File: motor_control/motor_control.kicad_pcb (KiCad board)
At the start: 4 copper layers, 75 x 56 mm, 28 parts, among them J1 GPIO, J2 MotA, J3 MotB, J4 MOT_POW, J5 UART, J6 SPI, J7 I2C, J8 VBUS_OUT, SW1 PU, SW2 PD, U1 HC-SR04

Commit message: add bear head logo
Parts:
- added G***: LOGO, LOGO, F.Cu at (111.4, 91.4)
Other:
- board text added: "Motor Control 25.08"

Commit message: adjust labels
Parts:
- A2: value Pololu_Breakout_TB6612FNG -> TB6612FNG
- A3: value RaspberryPi_Pico -> Raspberry Pi Pico
- renumbered D1 to BGKR
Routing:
- net /PULLUP: track 17.4 -> 23.9 mm
- net /PULLDOWN: track 16.2 -> 22.7 mm
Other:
- board text added: "+"
- board text added: "-"
- board text removed: "A1"
- board text removed: "A2"
- board text removed: "B1"
- board text removed: "B2"
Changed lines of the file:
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@@
 		)
 		(property "Value" "HC-SR04"
-			(at 23.8102 3.370695 90)
-			(layer "F.Fab")
+			(at 8.7 1.8 90)
+			(layer "F.SilkS")
 			(effects
 				(font
-					(size 1.001693 1.001693)
+					(size 1 1)
 					(thickness 0.15)
 				)
@@
 			)
 		)
-		(property "Value" "Pololu_Breakout_TB6612FNG"
-			(at 1.7955 -0.455 90)
-			(layer "F.Fab")
+		(property "Value" "TB6612FNG"
+			(at 0.0955 2.545 180)
+			(layer "F.SilkS")
 			(effects
 				(font
-					(size 0.640105 0.640105)
+					(size 0.8 0.8)
 					(thickness 0.15)
 				)
@@
 				(font
 					(size 1 1)
-					(thickness 0.15)
+					(thickness 0.2)
+					(bold yes)
 				)
 				(justify left)
 			)
 		)
-		(property "Value" "RaspberryPi_Pico"
+		(property "Value" "Raspberry Pi Pico"
 			(at 2.766 0.116 0)
 			(unlocked yes)
-			(layer "F.Fab")
+			(layer "F.SilkS")
 			(effects
 				(font
@@
 		(descr "LED, diameter 5.0mm, 4 pins, WP154A4, https://www.kingbright.com/attachments/file/psearch/000/00/00/L-154A4SUREQBFZGEW(Ver.11A).pdf")
 		(tags "LED diameter 5.0mm 2 pins diameter 5.0mm 3 pins diameter 5.0mm 4 pins RGB RGBLED")
-		(property "Reference" "D1"
-			(at 2.921 -3.937 0)
+		(property "Reference" "BGKR"
+			(at 3.12 -3.98 0)
 			(layer "F.SilkS")
 			(effects
@@
 		)
 		(property "Value" "LED_RKGB"
-			(at 3.2385 -3.937 0)
+			(at 2.92 -3.98 0)
 			(layer "F.Fab")
 			(effects
@@
 		(tags "Through hole pin header THT 1x02 2.54mm single row")
 		(property "Reference" "J8"
-			(at -2.6 3.6434 270)
+			(at 0.8 5.0434 0)
 			(layer "F.SilkS")
 			(effects
@@
 		(layer "Edge.Cuts")
 	)
-	(gr_text "A2"
-		(at 109.160691 58.5 0)
+	(gr_text "AO2"
+		(at 109 58.5 0)
 		(layer "F.SilkS")
 		(effects
@@
 		)
 	)
-	(gr_text "A1"
-		(at 96.460691 58.5 0)
+	(gr_text "AO1"
+		(at 96.2 58.5 0)
 		(layer "F.SilkS")
 		(effects
@@
 		)
 	)
-	(gr_text "VMOT"
-		(at 91.8 89.5 0)
+	(gr_text "+"
+		(at 91.8 89.3 0)
 		(layer "F.SilkS")
 		(effects
 			(font
-				(size 0.8 0.8)
+				(size 1 1)
 				(thickness 0.15)
 			)
@@
 		)
 	)
-	(gr_text "GND"
-		(at 94.9 89.5 0)
+	(gr_text "-"
+		(at 94.5 89.4 0)
 		(layer "F.SilkS")
 		(effects
 			(font
-				(size 0.8 0.8)
+				(size 1 1)
 				(thickness 0.15)
 			)
@@
 		)
 	)
-	(gr_text "B2"
-		(at 109.2 86.2 0)
+	(gr_text "BO2"
+		(at 108.9 86.2 0)
 		(layer "F.SilkS")
 		(effects
@@
 			(font
 				(size 1 1)
-				(thickness 0.15)
+				(thickness 0.2)
+				(bold yes)
 			)
 			(justify bottom)
@@
 	)
 	(gr_text "VBUS"
-		(at 159.005 82.9 0)
+		(at 159.3 82.9 0)
+		(layer "F.SilkS")
+		(effects
+			(font
+				(size 1 1)
+				(thickness 0.15)
+			)
+		)
+	)
+	(gr_text "GND"
+		(at 159.7 85.7 0)
 		(layer "F.SilkS")
 		(effects
@@
 		)
 	)
-	(gr_text "B1"
-		(at 96.5 86.2 0)
+	(gr_text "BO1"
+		(at 96.1 86.2 0)
 		(layer "F.SilkS")
 		(effects
@@
 	)
 	(segment
+		(start 118.64 93.6)
+		(end 125.14 93.6)
+		(width 0.2)
+		(layer "F.Cu")
+		(net 55)
+	)
+	(segment
 		(start 125.146 86.992)
 		(end 130.005 82.133)
@@
 	)
 	(segment
+		(start 128.8 93.6)
+		(end 135.3 93.6)
+		(width 0.2)
+		(layer "F.Cu")
+		(net 58)
+	)
+	(segment

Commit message: final tweak pcb
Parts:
- moved J4 2.93 mm to (97.3, 90.9)
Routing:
- net VMOT: track 18.8 -> 17.0 mm
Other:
- board text added: "JLCJLCJLC"
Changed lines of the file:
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@@
 	(footprint "Connector_PinHeader_2.54mm:PinHeader_1x02_P2.54mm_Horizontal"
 		(layer "F.Cu")
-		(at 94.4882 91.8974 -90)
+		(at 97.2545 90.945 -90)
 		(descr "Through hole angled pin header, 1x02, 2.54mm pitch, 6mm pin length, single row")
 		(tags "Through hole angled pin header THT 1x02 2.54mm single row")
 		(property "Reference" "J4"
-			(at 2.9026 -2.7178 180)
+			(at 2.755 5.3545 0)
 			(layer "F.SilkS")
 			(effects
@@
 		)
 		(property "Value" "MOT_POW"
-			(at -2.54 1.0922 180)
-			(layer "F.Fab")
+			(at -2.54 1.0922 0)
+			(layer "F.SilkS")
 			(effects
 				(font
@@
 		(tags "tact sw push 6mm")
 		(property "Reference" "SW1"
-			(at 3.25 2.25 0)
+			(at -3.04 5.4 0)
 			(layer "F.SilkS")
 			(effects
 				(font
-					(size 1 1)
+					(size 0.8 0.8)
 					(thickness 0.15)
 				)
@@
 		(tags "tact sw push 6mm")
 		(property "Reference" "SW2"
-			(at 3.25 2.25 0)
+			(at -2.8 -1 0)
 			(layer "F.SilkS")
 			(effects
 				(font
-					(size 1 1)
+					(size 0.8 0.8)
 					(thickness 0.15)
 				)
@@
 		(tags "LED diameter 5.0mm 2 pins diameter 5.0mm 3 pins diameter 5.0mm 4 pins RGB RGBLED")
 		(property "Reference" "BGKR"
-			(at 3.12 -3.98 0)
+			(at 1.72 -3.98 0)
 			(layer "F.SilkS")
 			(effects
@@
 	)
 	(gr_text "+"
-		(at 91.8 89.3 0)
+		(at 92.1 89.5 0)
 		(layer "F.SilkS")
 		(effects
@@
 	)
 	(gr_text "-"
-		(at 94.5 89.4 0)
+		(at 100 89.4 0)
 		(layer "F.SilkS")
 		(effects
@@
 	)
 	(gr_text "Motor Control\n25.08"
-		(at 112 97.9 0)
+		(at 111.9 97.9 0)
 		(layer "F.SilkS")
 		(effects
@@
 		)
 	)
+	(gr_text "JLCJLCJLC"
+		(at 107.4 92.7 0)
+		(layer "B.SilkS")
+		(effects
+			(font
+				(size 1 1)
+				(thickness 0.15)
+			)
+			(justify left bottom mirror)
+		)
+	)
 	(gr_text "USB"
 		(at 177.724 71.552 0)
@@
 	)
 	(segment
-		(start 95.4 88.4456)
-		(end 95.4 76.9)
+		(start 95.5645 77.395)
+		(end 97.2545 75.705)
 		(width 0.4)
 		(layer "B.Cu")
@@
 	)
 	(segment
-		(start 95.4 76.9)
-		(end 96.595 75.705)
+		(start 94.7145 90.945)
+		(end 95.5645 90.095)
 		(width 0.4)
 		(layer "B.Cu")
@@
 	)
 	(segment
-		(start 91.9482 91.8974)
-		(end 95.4 88.4456)
+		(start 95.5645 90.095)
+		(end 95.5645 77.395)
 		(width 0.4)
 		(layer "B.Cu")

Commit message: export gerber
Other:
- board text added: "JLCJLCJLCJLC"
- board text removed: "JLCJLCJLC"
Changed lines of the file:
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@@
 		(grid_origin 100 100)
 		(pcbplotparams
-			(layerselection 0x00000000_00000000_00000000_000000a5)
+			(layerselection 0x00000000_00000000_55555555_5755f5af)
 			(plot_on_all_layers_selection 0x00000000_00000000_00000000_00000000)
 			(disableapertmacros no)
@@
 			(sketchdnponfab yes)
 			(crossoutdnponfab yes)
-			(subtractmaskfromsilk no)
+			(subtractmaskfromsilk yes)
 			(outputformat 1)
 			(mirror no)
-			(drillshape 1)
+			(drillshape 0)
 			(scaleselection 1)
-			(outputdirectory "")
+			(outputdirectory "jlcpcb_gerbers/")
 		)
 	)
@@
 		)
 	)
-	(gr_text "JLCJLCJLC"
-		(at 107.4 92.7 0)
+	(gr_text "JLCJLCJLCJLC"
+		(at 91.4 55.8 270)
 		(layer "B.SilkS")
 		(effects

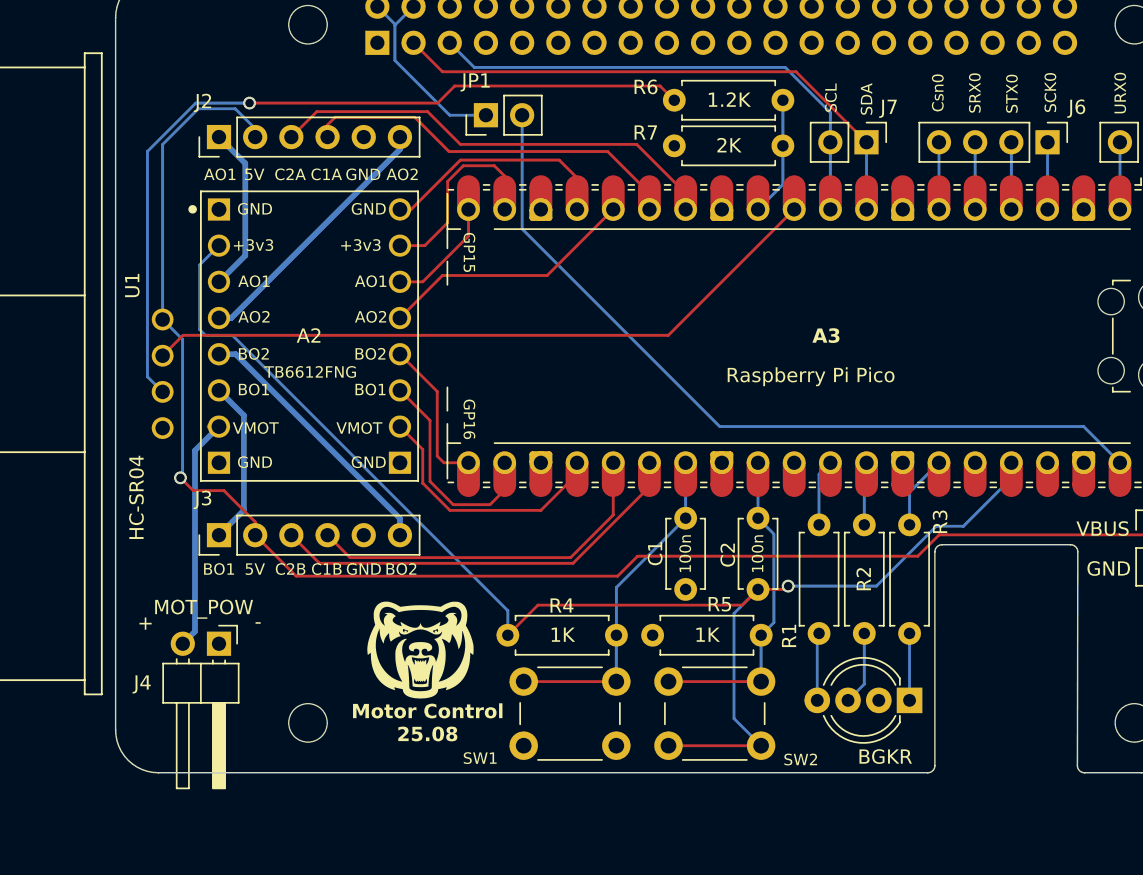
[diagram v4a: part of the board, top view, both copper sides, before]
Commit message: update schematic and pcb
1. added a input 01x02 header for PEB power up +5V
2. switched to +5V to power up sonar and encoders
3. set jumper between +5V and PEB 5V input
4. upgraded motor driver input to JST-XH
5. updated footprints
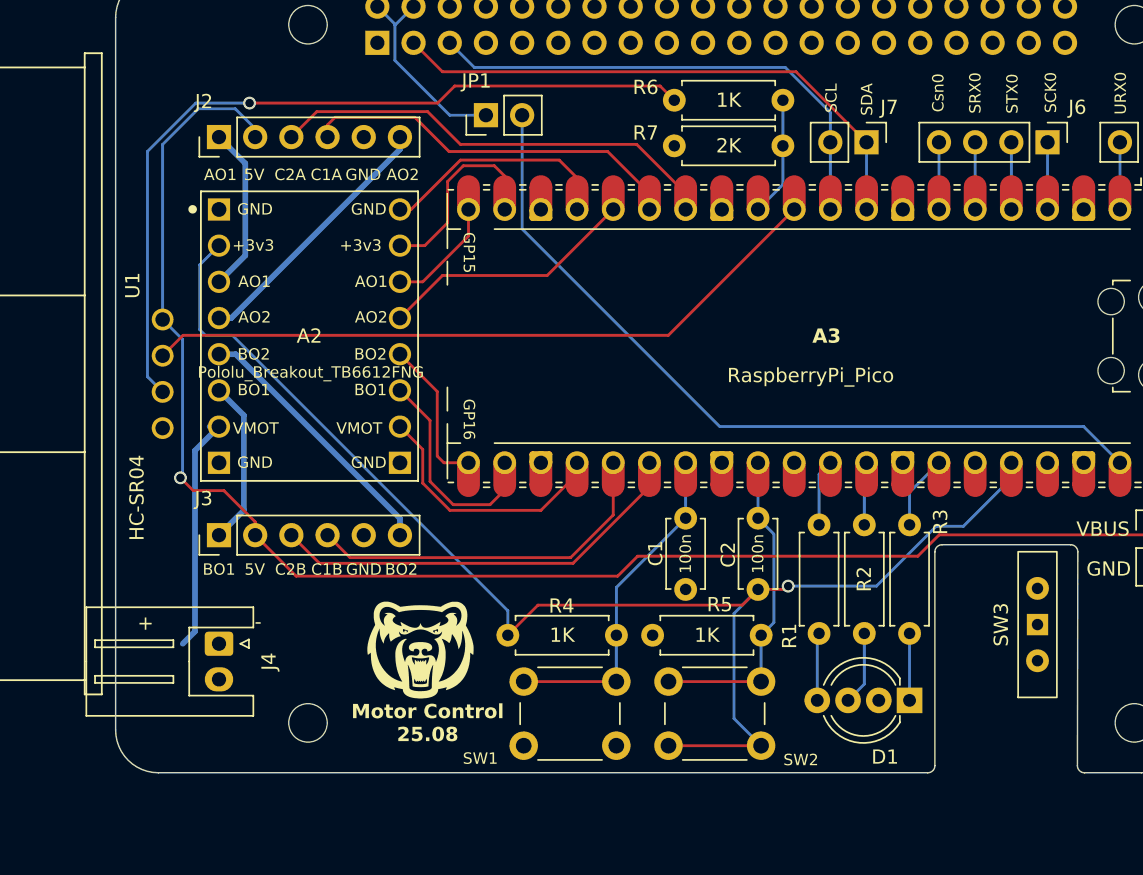
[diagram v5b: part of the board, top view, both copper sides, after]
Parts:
- added SW3: SW_SPDT_312, Button_Switch_THT:SW_Slide-03_Wuerth-WS-SLTV_10x2.5x6.4_P2.54mm, F.Cu at (154.7, 89.6)
- A2: value TB6612FNG -> Pololu_Breakout_TB6612FNG
- A3: value Raspberry Pi Pico -> RaspberryPi_Pico
- J4: footprint Connector_PinHeader_2.54mm:PinHeader_1x02_P2.54mm_Horizontal -> Connector_JST:JST_XH_S2B-XH-A_1x02_P2.50mm_Horizontal
- J8: value VBUS_OUT -> PEB_5V_IN
- JP1: value 5V_VBUS -> 5V_PEB_RPi
- R6: value 1.2K -> 1K
- renumbered BGKR to D1
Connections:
- J2 pad 2: VBUS -> +5V
- J3 pad 2: VBUS -> +5V
- J8 pad 1: VBUS -> 5V_IN
- JP1 pad 1: +5V -> 5V_IN
- JP1 pad 2: VSYS -> +5V
- R7 pad 1: GND -> Net-(U1-ECHO)
- R7 pad 2: /ECHO -> GND
- U1 pad 1: VBUS -> +5V

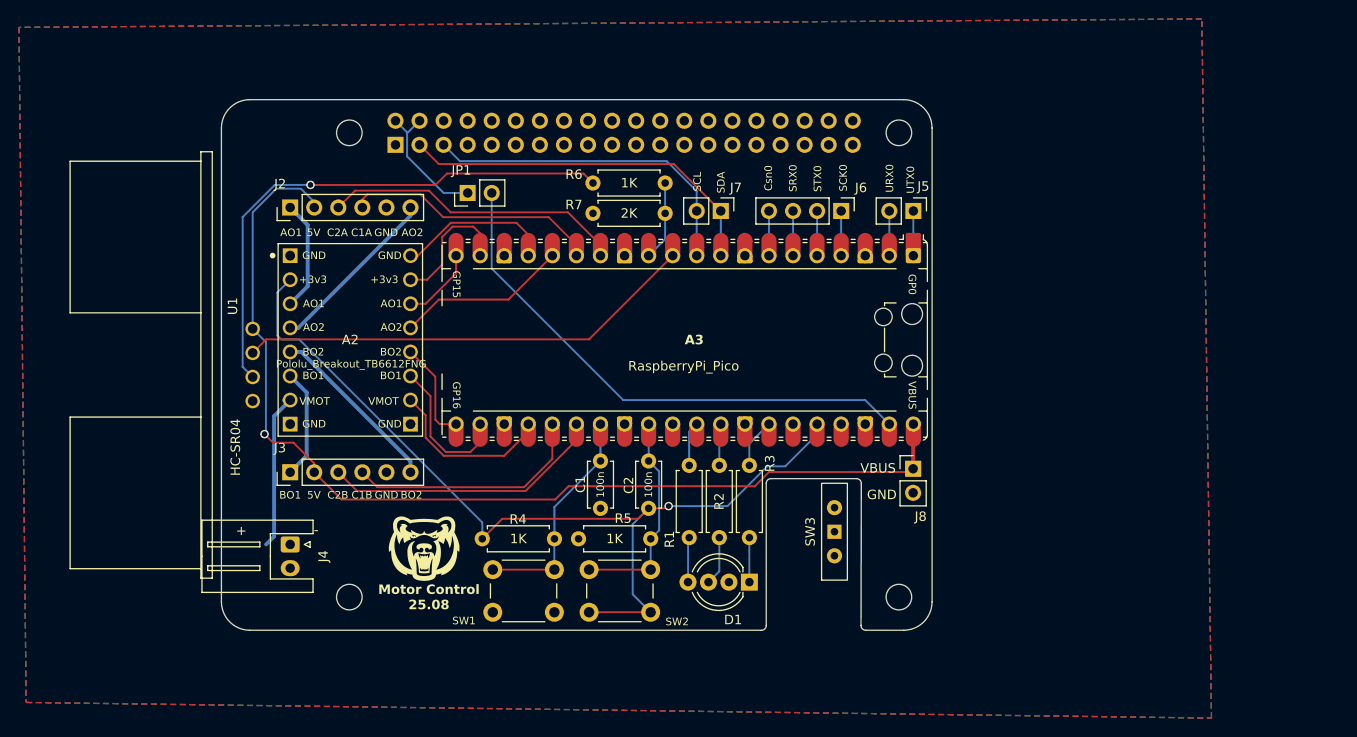
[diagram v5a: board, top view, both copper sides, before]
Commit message: fix j9 footprint and update pcb
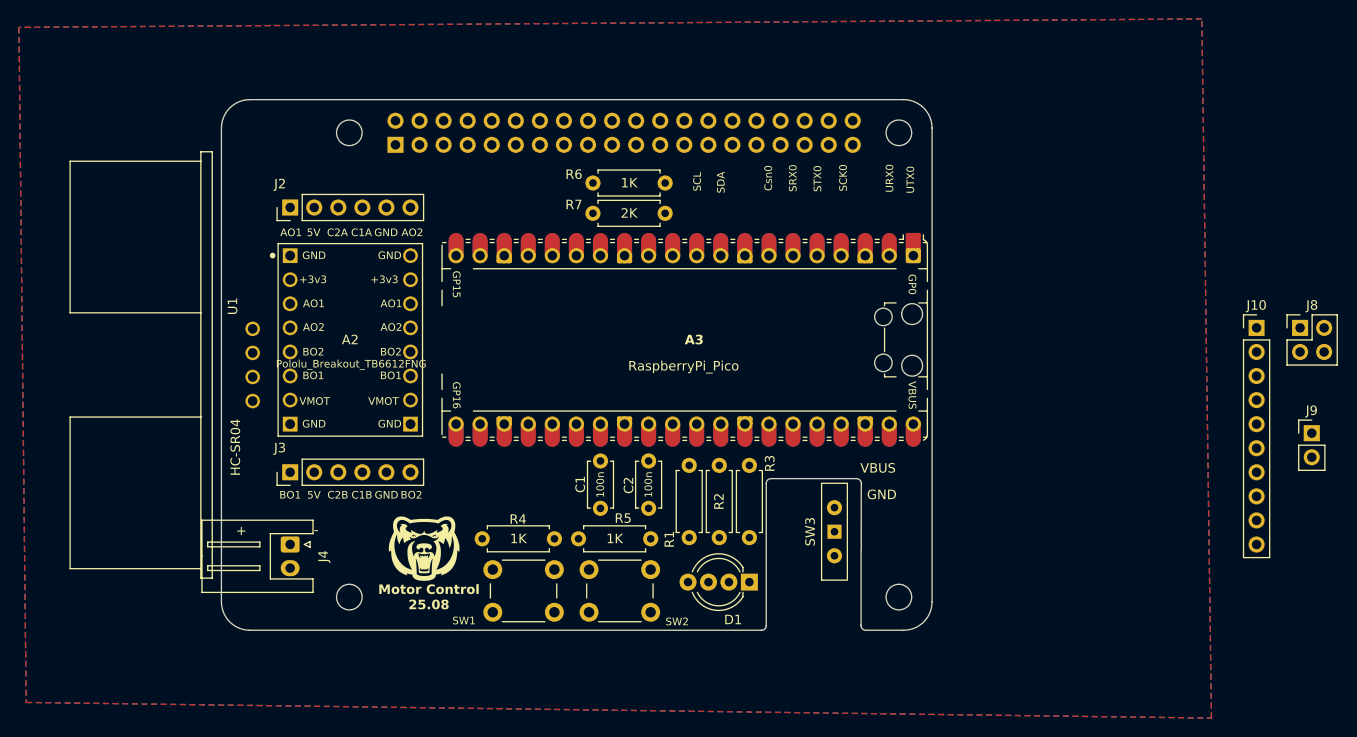
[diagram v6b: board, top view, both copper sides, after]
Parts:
- removed J5: UART, Connector_PinHeader_2.54mm:PinHeader_1x02_P2.54mm_Vertical
- removed J6: SPI, Connector_PinHeader_2.54mm:PinHeader_1x04_P2.54mm_Vertical
- removed J7: I2C, Connector_PinHeader_2.54mm:PinHeader_1x02_P2.54mm_Vertical
- removed JP1: 5V_PEB_RPi, Connector_PinHeader_2.54mm:PinHeader_1x02_P2.54mm_Vertical
- added J10: Conn_01x10_Pin, Connector_PinHeader_2.54mm:PinHeader_1x10_P2.54mm_Vertical, F.Cu at (199.2, 68.1)
- added J9: VBUS_OUT, Connector_PinHeader_2.54mm:PinHeader_1x02_P2.54mm_Vertical, F.Cu at (205.1, 79.2)
- J8: value PEB_5V_IN -> Conn_02x02_Odd_Even; footprint Connector_PinHeader_2.54mm:PinHeader_1x02_P2.54mm_Vertical -> Connector_PinHeader_2.54mm:PinHeader_2x02_P2.54mm_Vertical
- moved J8 43.5 mm to (203.8, 68.1)
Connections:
- A3 pad 1: /UART0_TX -> /GP0
- A3 pad 10: /SCL1 -> /GP7
- A3 pad 16: /STBY -> /PWMA
- A3 pad 17: /PWMA -> /AIN2
- A3 pad 19: /AIN2 -> /AIN1
- A3 pad 2: /UART0_RX -> /GP1
- A3 pad 20: /AIN1 -> /STBY
- A3 pad 25: /C1B -> /C2B
- A3 pad 26: /C2B -> /C1B
- A3 pad 4: /SPI0_SCK -> /GP2
- A3 pad 5: /SPI0_TX -> /GP3
- A3 pad 6: /SPI0_RX -> /GP4
- A3 pad 7: /SPI0_CSn -> /GP5
- A3 pad 9: /SDA1 -> /GP6
- C1 pad 1: GND -> /PULLUP
- C1 pad 2: /PULLUP -> GND
- C2 pad 1: /PULLDOWN -> GND
- C2 pad 2: +3V3 -> /PULLDOWN
- J2 pad 2: +5V -> REG_5V
- J3 pad 2: +5V -> REG_5V
- J8 pad 1: 5V_IN -> GND
- J8 pad 2: GND -> REG_5V
- SW1 pad 1: /PULLUP -> GND
- SW1 pad 2: GND -> /PULLUP
- SW3 pad 1: 5V_IN -> REG_5V
- U1 pad 1: +5V -> REG_5V
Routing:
- net VBUS: track 110.7 -> 0.00 mm, vias 1 -> 0
- net +3V3: track 97.9 -> 0.00 mm, vias 1 -> 0
- net Net-(U1-ECHO): track 56.9 -> 0.00 mm, vias 1 -> 0
- net VSYS: track 56.7 -> 0.00 mm
- net /TRIG: track 48.6 -> 0.00 mm
- net /SDA1: track 39.4 -> 0.00 mm
- net /SCL1: track 35.5 -> 0.00 mm
- net /C2A: track 31.9 -> 0.00 mm
- net /C2B: track 29.2 -> 0.00 mm
- net /C1A: track 27.0 -> 0.00 mm
- net /C1B: track 24.8 -> 0.00 mm
- net /PULLUP: track 23.9 -> 0.00 mm
- net /PULLDOWN: track 22.7 -> 0.00 mm
- net /BO2: track 18.6 -> 0.00 mm
- net /AO2: track 18.5 -> 0.00 mm
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
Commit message: update motor connector pins
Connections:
- J2 pad 3: /C2A -> /C1A
- J2 pad 4: /C1A -> /C2A
- J3 pad 1: /BO1 -> /BO2
- J3 pad 3: /C2B -> /C1B
- J3 pad 4: /C1B -> /C2B
- J3 pad 6: /BO2 -> /BO1
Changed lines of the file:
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@@
 			(layers "*.Cu" "*.Mask")
 			(remove_unused_layers no)
-			(net 40 "/BO1")
+			(net 32 "/BO2")
 			(pinfunction "Pin_1")
 			(pintype "passive")
@@
 			(layers "*.Cu" "*.Mask")
 			(remove_unused_layers no)
-			(net 65 "/C2B")
+			(net 60 "/C1B")
 			(pinfunction "Pin_3")
 			(pintype "passive")
@@
 			(layers "*.Cu" "*.Mask")
 			(remove_unused_layers no)
-			(net 60 "/C1B")
+			(net 65 "/C2B")
 			(pinfunction "Pin_4")
 			(pintype "passive")
@@
 			(layers "*.Cu" "*.Mask")
 			(remove_unused_layers no)
-			(net 32 "/BO2")
+			(net 40 "/BO1")
 			(pinfunction "Pin_6")
 			(pintype "passive")
@@
 			(layers "*.Cu" "*.Mask")
 			(remove_unused_layers no)
-			(net 59 "/C2A")
+			(net 44 "/C1A")
 			(pinfunction "Pin_3")
 			(pintype "passive")
@@
 			(layers "*.Cu" "*.Mask")
 			(remove_unused_layers no)
-			(net 44 "/C1A")
+			(net 59 "/C2A")
 			(pinfunction "Pin_4")
 			(pintype "passive")

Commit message: update layout
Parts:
- moved J8 94.9 mm to (112.8, 95.0), turned to -90 degrees
- moved SW3 45.0 mm to (109.7, 90.3), turned to 0 degrees
- moved J4 41.5 mm to (96.5, 49.5), turned to 180 degrees
- moved J10 38.9 mm to (163.0, 54.1), turned to -90 degrees
- moved J9 32.6 mm to (172.5, 80.1)
- moved G*** 16.3 mm to (95.2, 91.0)
- moved SW1 7.52 mm to (124.5, 98.3), turned to 180 degrees
- moved R7 4.03 mm to (129.2, 52.0)
- moved R6 2.35 mm to (129.1, 55.1)
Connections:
- A3 pad 16: /PWMA -> /STBY
- A3 pad 17: /AIN2 -> /AIN1
- A3 pad 19: /AIN1 -> /AIN2
- A3 pad 20: /STBY -> /PWMA
- A3 pad 21: /BIN1 -> /PWMB
- A3 pad 24: /PWMB -> /BIN1
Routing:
- net /C1A: track 0.00 -> 1.13 mm
